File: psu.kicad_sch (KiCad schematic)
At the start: 7 parts, among them J1 Screw_Terminal_01x02, U1 L78L05_TO92

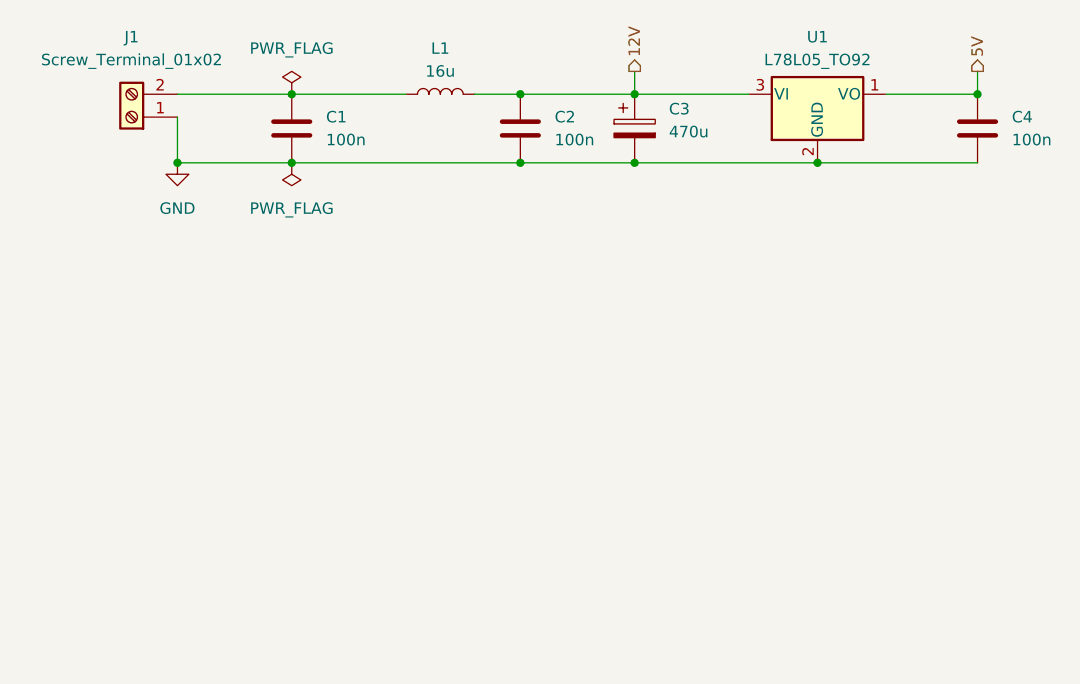
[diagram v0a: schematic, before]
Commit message: Rework RF amplifier design and add AF amplification
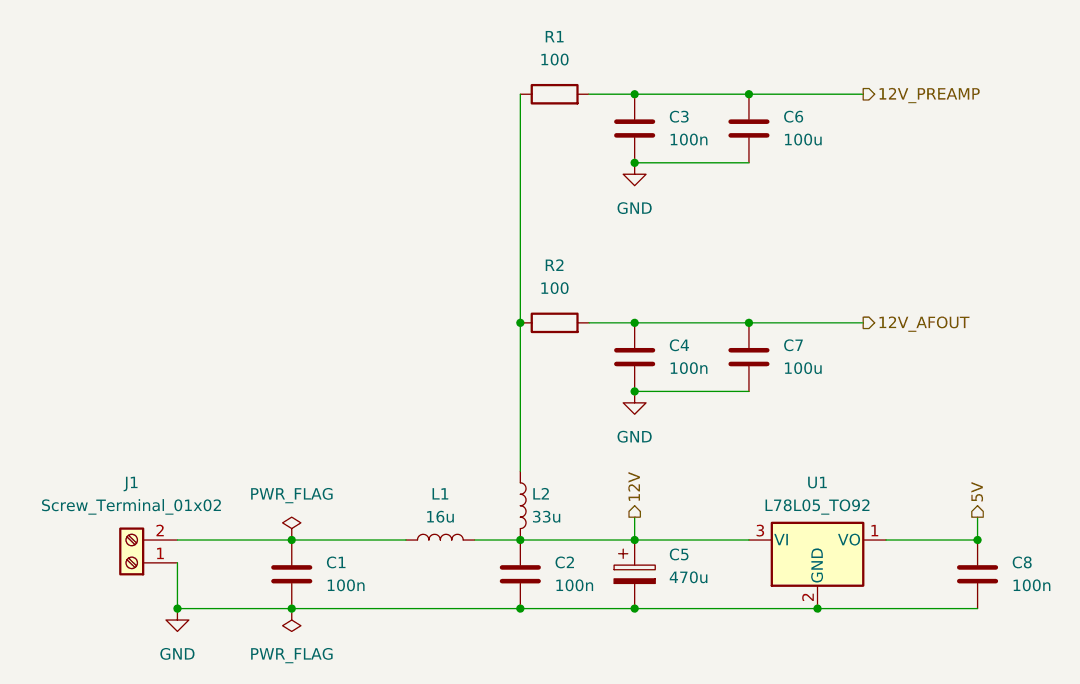
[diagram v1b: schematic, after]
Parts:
- added C3, C4: 100n, symbol Device:C
- added C6, C7: 100u, symbol Device:C
- added L2: 33u, symbol Device:L
- added R1, R2: 100, symbol Device:R
- renumbered C3 to C5, C4 to C8
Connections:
- net 12V: now also L2.2
- net GND: now also C3.1, C4.1, C6.1, C7.1
- new net: L2.1, R1.1, R2.1
- new net 12V_AFOUT: C4.2, C7.2, R2.2
- new net 12V_PREAMP: C3.2, C6.2, R1.2
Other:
- moved on the sheet: C1, C2, C5, C8, J1, L1, U1
